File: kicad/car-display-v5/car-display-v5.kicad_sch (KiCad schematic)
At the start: 52 parts, among them J1 AVRISP-6, J2 Screw_Terminal_01x03, J3 PicoBlade F 1x7, J4 Socket 1x6 0.1", J5 JMP 1x3 0.05", U1 ATmega328PB-M, U2 TXS0108ERGYR, U3 MCP25625T-E/ML, U4 TPSM365R3RDNR, U5 LP3988*-*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

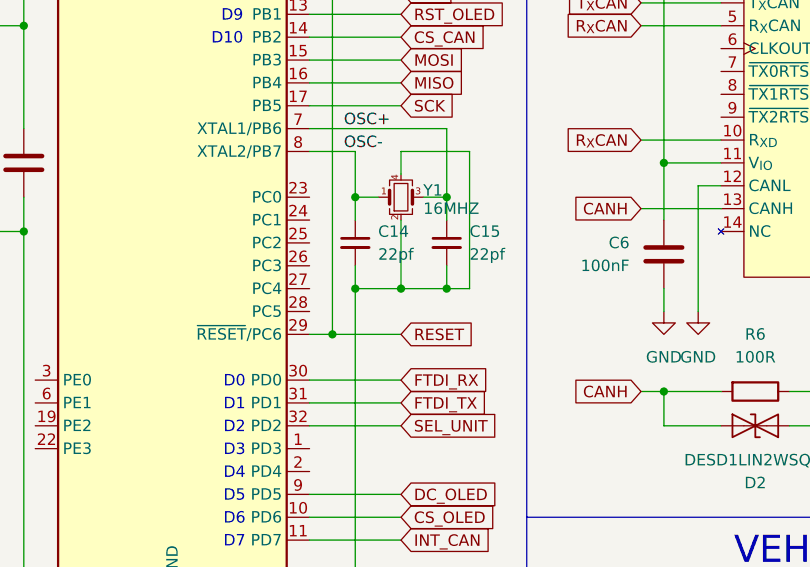
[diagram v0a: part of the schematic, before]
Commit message: Add 3.3V PGOOD trace
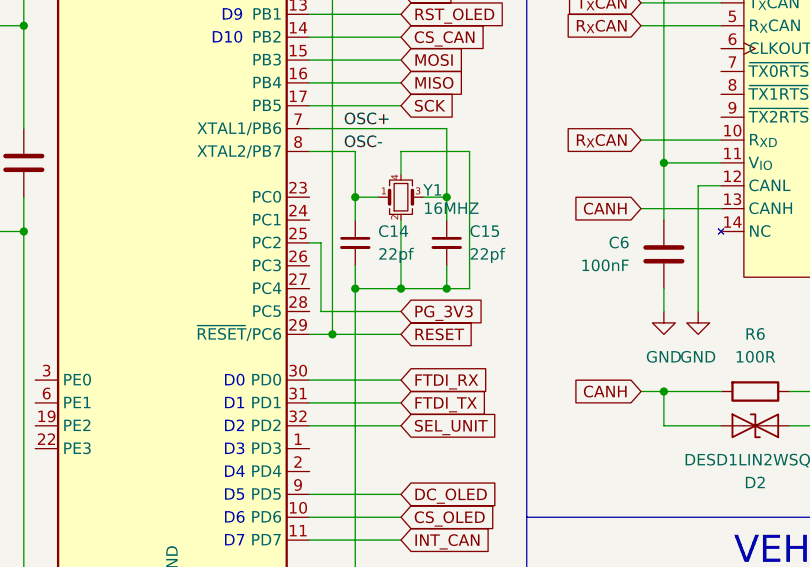
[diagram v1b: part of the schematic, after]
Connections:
- net PG_3V3: now also U1.25 (PC2)
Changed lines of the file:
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@@
+	(wire
+		(pts
+			(xy 55.88 73.66) (xy 64.77 73.66)
+		)
+		(stroke
+			(width 0)
+			(type default)
+		)
+	)
 	(wire
 		(pts
@@
 	(wire
 		(pts
+			(xy 54.61 66.04) (xy 55.88 66.04)
+		)
+		(stroke
+			(width 0)
+			(type default)
+		)
+	)
+	(wire
+		(pts
 			(xy 252.73 40.64) (xy 252.73 48.26)
 		)
@@
 		(pts
 			(xy 50.8 130.81) (xy 50.8 133.35)
+		)
+		(stroke
+			(width 0)
+			(type default)
+		)
+	)
+	(wire
+		(pts
+			(xy 55.88 66.04) (xy 55.88 73.66)
 		)
 		(stroke
@@
 			(effects
 				(font
+					(size 1.27 1.27)
+				)
+				(justify left)
+				(hide yes)
+			)
+		)
+	)
+	(global_label "PG_3V3"
+		(shape input)
+		(at 64.77 73.66 0)
+		(fields_autoplaced yes)
+		(effects
+			(font
+				(size 1.27 1.27)
+			)
+			(justify left)
+		)
+		(property "Intersheetrefs" "${INTERSHEET_REFS}"
+			(at 74.7704 73.66 0)
+			(effects
+				(font

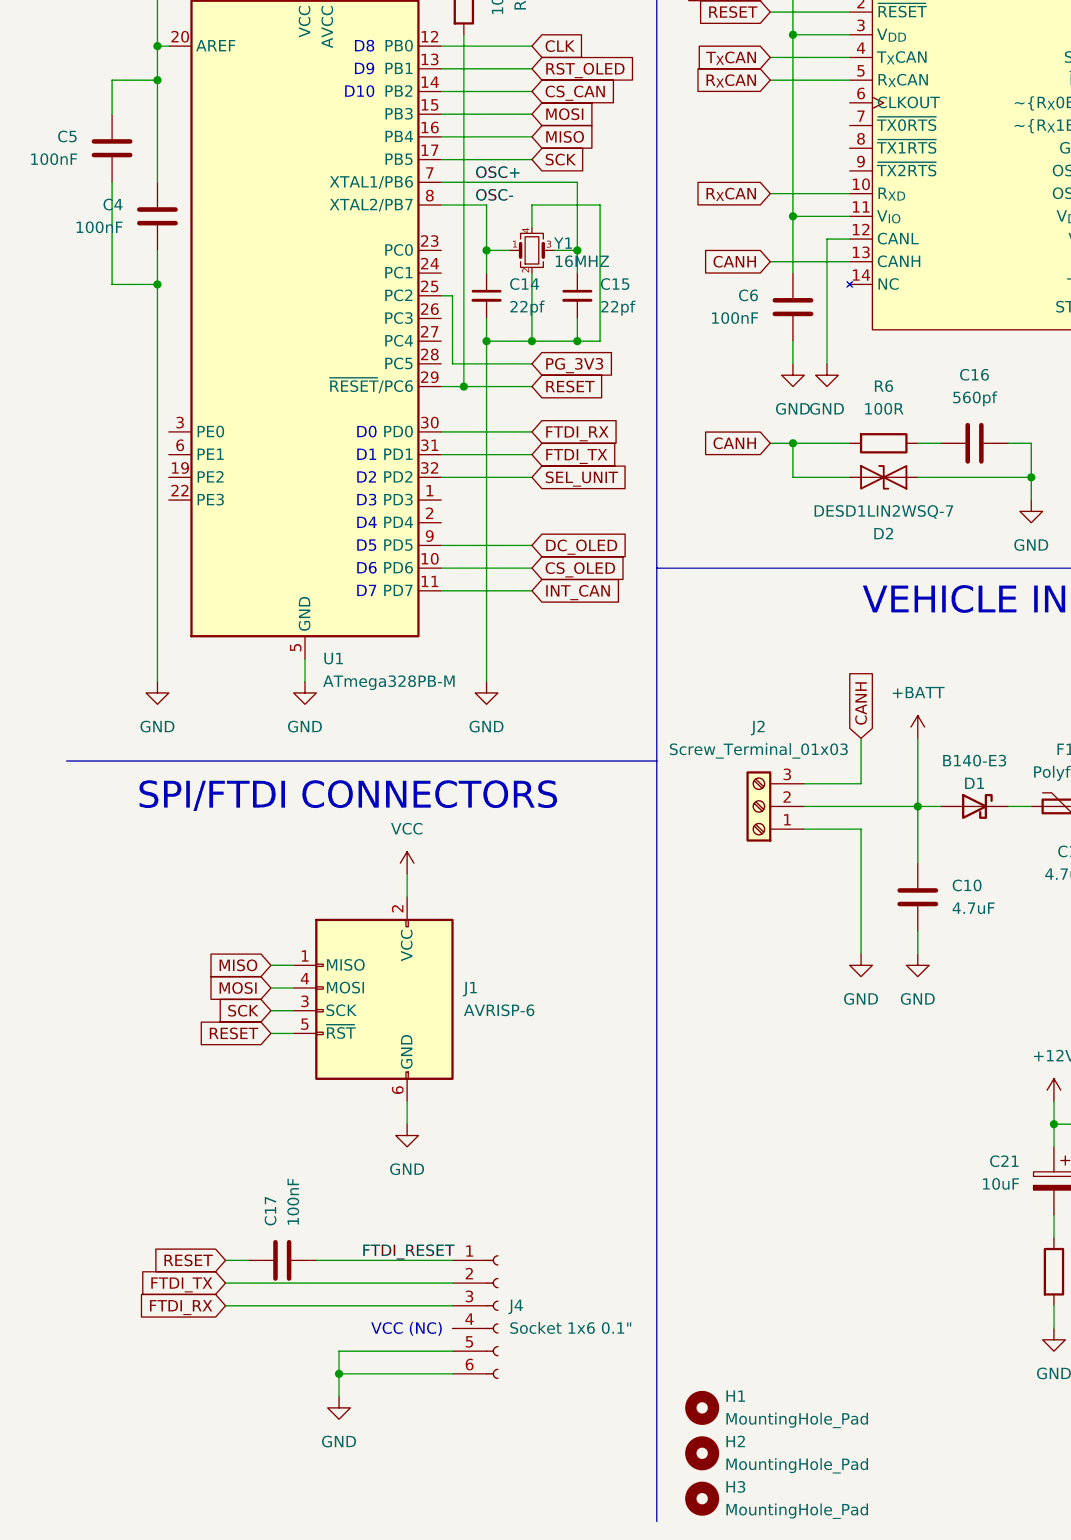
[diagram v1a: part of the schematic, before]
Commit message: Move OLED connector to side opposite of CAN input
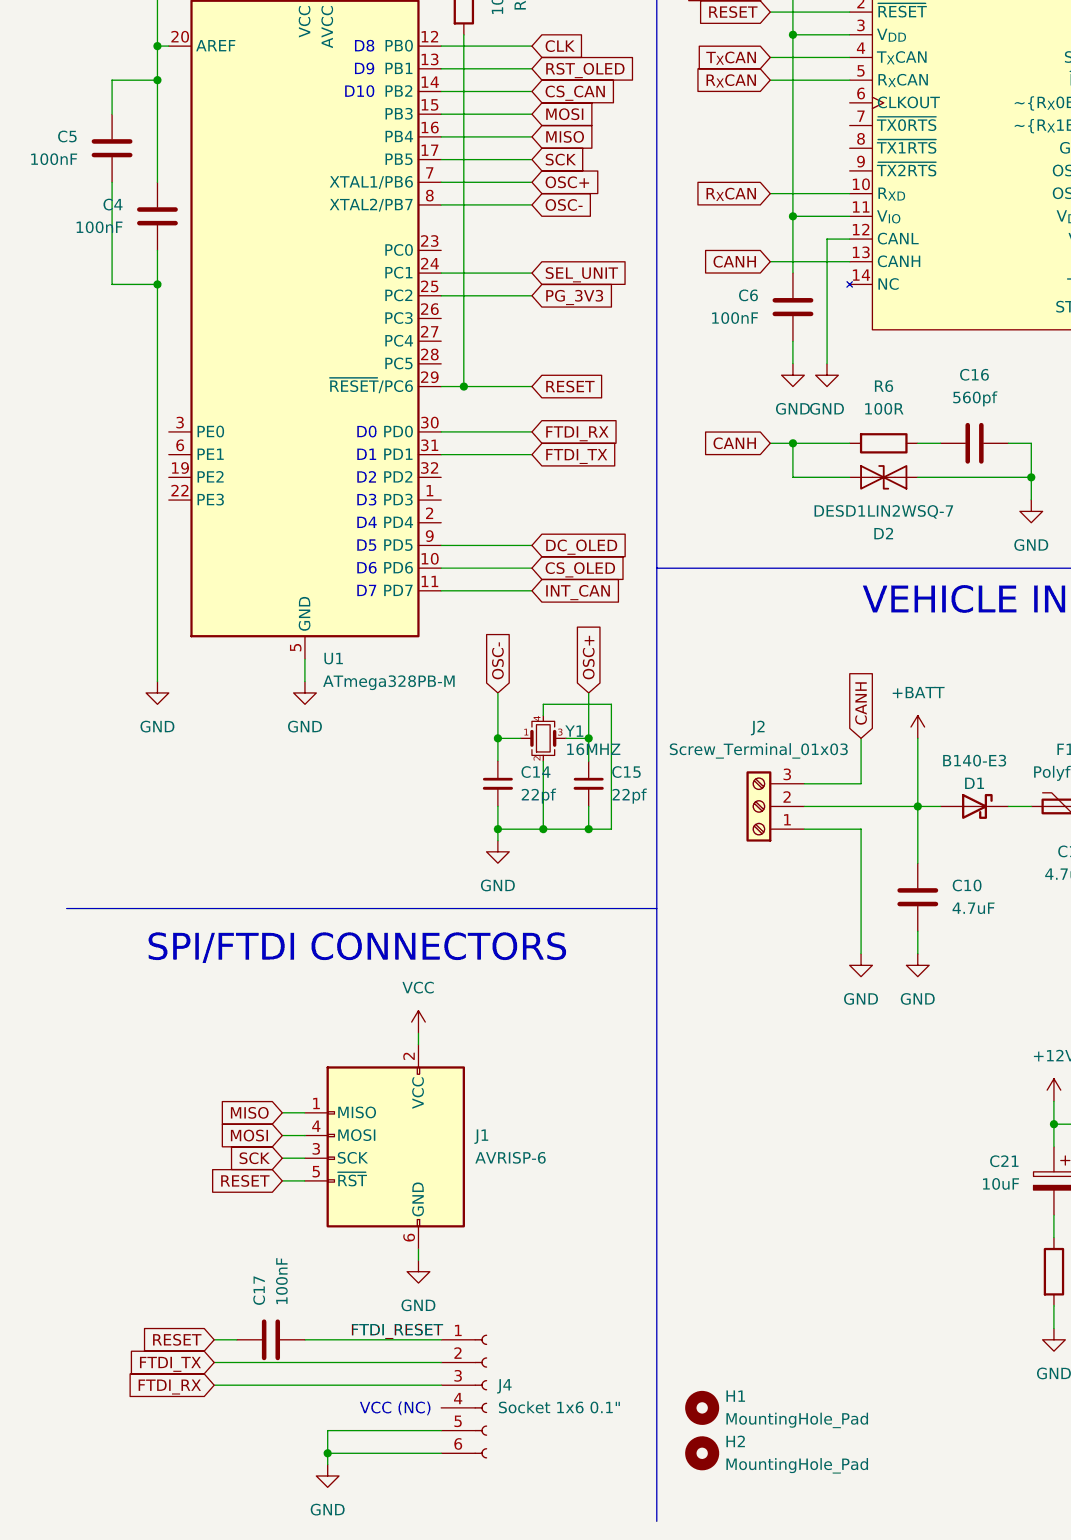
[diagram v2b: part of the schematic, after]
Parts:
- removed H3: MountingHole_Pad, MountingHole:MountingHole_2.2mm_M2_DIN965, symbol Mechanical:MountingHole
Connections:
- net SEL_UNIT: now also U1.24 (PC1); no longer U1.32 (PD2)
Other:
- moved on the sheet: C14, C15, C17, J1, J4, Y1

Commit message: Updates
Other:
- note added: "16"
- note added: "17"
- note added: "23/SDA1"
- note added: "24/SCL1"
- note added: "25/SS1"
- note added: "26/MOSI1"
- note added: "4"
- note added: "7"
- note added: "8"
- note added: "INT0/2"
- note added: "INT1/3"
- note added: "MISO/12"
- note added: "MISO1/14"
- note added: "OC0A/6"
- note added: "OC0B/5"
- note added: "OC1A/9"
- note added: "OC1B/SS/10"
- note added: "OC2A/MOSI/11"
- note added: "RXD/1"
- note added: "SCK/13"
- note added: "SCK1/15"
- note added: "SCL/19"
- note added: "SDA/18"
- note added: "TXD/0"
- note removed: "D0"
- note removed: "D1"
- note removed: "D10"
- note removed: "D2"
- note removed: "D3"
- note removed: "D4"
- note removed: "D5"
- note removed: "D6"
- note removed: "D7"
- note removed: "D8"
- note removed: "D9"
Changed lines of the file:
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@@
 	(wire
 		(pts
+			(xy 245.11 27.94) (xy 245.11 30.48)
+		)
+		(stroke
+			(width 0)
+			(type default)
+		)
+	)
+	(wire
+		(pts
 			(xy 54.61 96.52) (xy 64.77 96.52)
 		)
@@
 	(wire
 		(pts
-			(xy 245.11 27.94) (xy 245.11 30.48)
-		)
-		(stroke
-			(width 0)
-			(type default)
-		)
-	)
-	(wire
-		(pts
 			(xy 172.72 50.8) (xy 172.72 66.04)
 		)
@@
 	(wire
 		(pts
-			(xy 170.18 40.64) (xy 196.85 40.64)
+			(xy 167.64 40.64) (xy 196.85 40.64)
 		)
 		(stroke
@@
 		)
 	)
-	(text "D5"
+	(text "23/SDA1"
+		(exclude_from_sim no)
+		(at 30.988 81.534 0)
+		(effects
+			(font
+				(size 1.27 1.27)
+			)
+			(justify left)
+		)
+	)
+	(text "OC0B/5"
 		(exclude_from_sim no)
 		(at 47.498 94.234 0)
@@
 		)
 	)
-	(text "D3\n"
+	(text "INT1/3\n"
 		(exclude_from_sim no)
 		(at 47.498 89.154 0)
@@
 		)
 	)
-	(text "D1"
+	(text "RXD/1"
 		(exclude_from_sim no)
 		(at 47.498 84.074 0)
@@
 		)
 	)
-	(text "D2"
+	(text "INT0/2"
 		(exclude_from_sim no)
 		(at 47.498 86.614 0)
@@
 		)
 	)
-	(text "D8\n"
+	(text "SCK1/15"
+		(exclude_from_sim no)
+		(at 47.498 63.754 0)
+		(effects
+			(font
+				(size 1.27 1.27)
+			)
+			(justify right)
+		)
+	)
+	(text "8\n"
 		(exclude_from_sim no)
 		(at 47.244 38.354 0)
@@
 		)
 	)
-	(text "D10"
+	(text "17"
+		(exclude_from_sim no)
+		(at 47.498 68.834 0)
+		(effects
+			(font
+				(size 1.27 1.27)
+			)
+			(justify right)
+		)
+	)
+	(text "OC1B/SS/10"
 		(exclude_from_sim no)
 		(at 47.244 43.434 0)
@@
 		)
 	)
-	(text "D6"
+	(text "OC0A/6"
 		(exclude_from_sim no)
 		(at 47.498 96.774 0)
@@
 		)
 	)
-	(text "D0"
+	(text "SCL/19"
+		(exclude_from_sim no)
+		(at 47.498 73.914 0)
+		(effects
+			(font
+				(size 1.27 1.27)
+			)
+			(justify right)
+		)
+	)
+	(text "16"
+		(exclude_from_sim no)
+		(at 47.498 66.294 0)
+		(effects
+			(font
+				(size 1.27 1.27)
+			)
+			(justify right)
+		)
+	)
+	(text "24/SCL1"
+		(exclude_from_sim no)
+		(at 30.988 84.074 0)
+		(effects
+			(font
+				(size 1.27 1.27)
+			)
+			(justify left)
+		)
+	)
+	(text "SCK/13"
+		(exclude_from_sim no)
+		(at 47.244 51.054 0)
+		(effects
+			(font
+				(size 1.27 1.27)
+			)
+			(justify right)
+		)
+	)
+	(text "TXD/0"
 		(exclude_from_sim no)
 		(at 47.498 81.534 0)
@@
 		)
 	)
-	(text "D7"
+	(text "SDA/18"
+		(exclude_from_sim no)
+		(at 47.498 71.374 0)
+		(effects
+			(font
+				(size 1.27 1.27)
+			)
+			(justify right)
+		)
+	)
+	(text "7"
 		(exclude_from_sim no)
 		(at 47.498 99.314 0)
@@
 		)
 	)
+	(text "26/MOSI1"
+		(exclude_from_sim no)
+		(at 30.988 89.154 0)
+		(effects
+			(font
+				(size 1.27 1.27)
+			)
+			(justify left)
+		)
+	)
 	(text "SPI/FTDI CONNECTORS"
 		(exclude_from_sim no)
@@
 		)
 	)
-	(text "D9\n"
+	(text "MISO/12"
+		(exclude_from_sim no)
+		(at 47.244 48.514 0)
+		(effects
+			(font
+				(size 1.27 1.27)
+			)
+			(justify right)
+		)
+	)
+	(text "OC1A/9\n"
 		(exclude_from_sim no)
 		(at 47.244 40.894 0)
@@
 		)
 	)
-	(text "D4\n"
+	(text "MISO1/14"
+		(exclude_from_sim no)
+		(at 47.498 61.214 0)
+		(effects
+			(font
+				(size 1.27 1.27)
+			)
+			(justify right)
+		)
+	)
+	(text "25/SS1"
+		(exclude_from_sim no)
+		(at 30.988 86.614 0)
+		(effects
+			(font
+				(size 1.27 1.27)
+			)
+			(justify left)
+		)
+	)
+	(text "4"
 		(exclude_from_sim no)
 		(at 47.498 91.694 0)
@@
 		)
 	)
+	(text "OC2A/MOSI/11"
+		(exclude_from_sim no)
+		(at 47.244 45.974 0)
+		(effects
+			(font
+				(size 1.27 1.27)
+			)
+			(justify right)
+		)
+	)
 	(text "OLED CONN / FB / LEVEL SHIFT"
 		(exclude_from_sim no)
@@
 	(global_label "PG_5V"
 		(shape input)
-		(at 170.18 40.64 180)
+		(at 167.64 40.64 180)
 		(fields_autoplaced yes)
 		(effects
@@
 		)
 		(property "Intersheetrefs" "${INTERSHEET_REFS}"
-			(at 161.3891 40.64 0)
+			(at 158.8491 40.64 0)
 			(effects
 				(font
@@
 			)
 		)
-		(property "Description" ""
+		(property "Description" "C1608X7R1V105K080AC"
 			(at 158.75 97.79 0)
 			(effects
@@
 			)
 		)
-		(property "Description" ""
+		(property "Description" "GRM31CR71H475KA12L"
 			(at 107.95 133.35 0)
 			(effects
@@
 			)
 		)
-		(property "Description" ""
+		(property "Description" "GRM31CR71H475KA12L"
 			(at 140.97 133.35 0)
 			(effects
@@
 			)
 		)
-		(property "Description" ""
+		(property "Description" "GRM31CR71H475KA12L"
 			(at 130.81 129.54 0)
 			(effects
